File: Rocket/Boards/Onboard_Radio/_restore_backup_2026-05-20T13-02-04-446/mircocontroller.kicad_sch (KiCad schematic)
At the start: 32 parts, among them J3 USB_B_Micro, J4 SWD JST PH, U4 STM32H562RGT6, Y2 12MHz

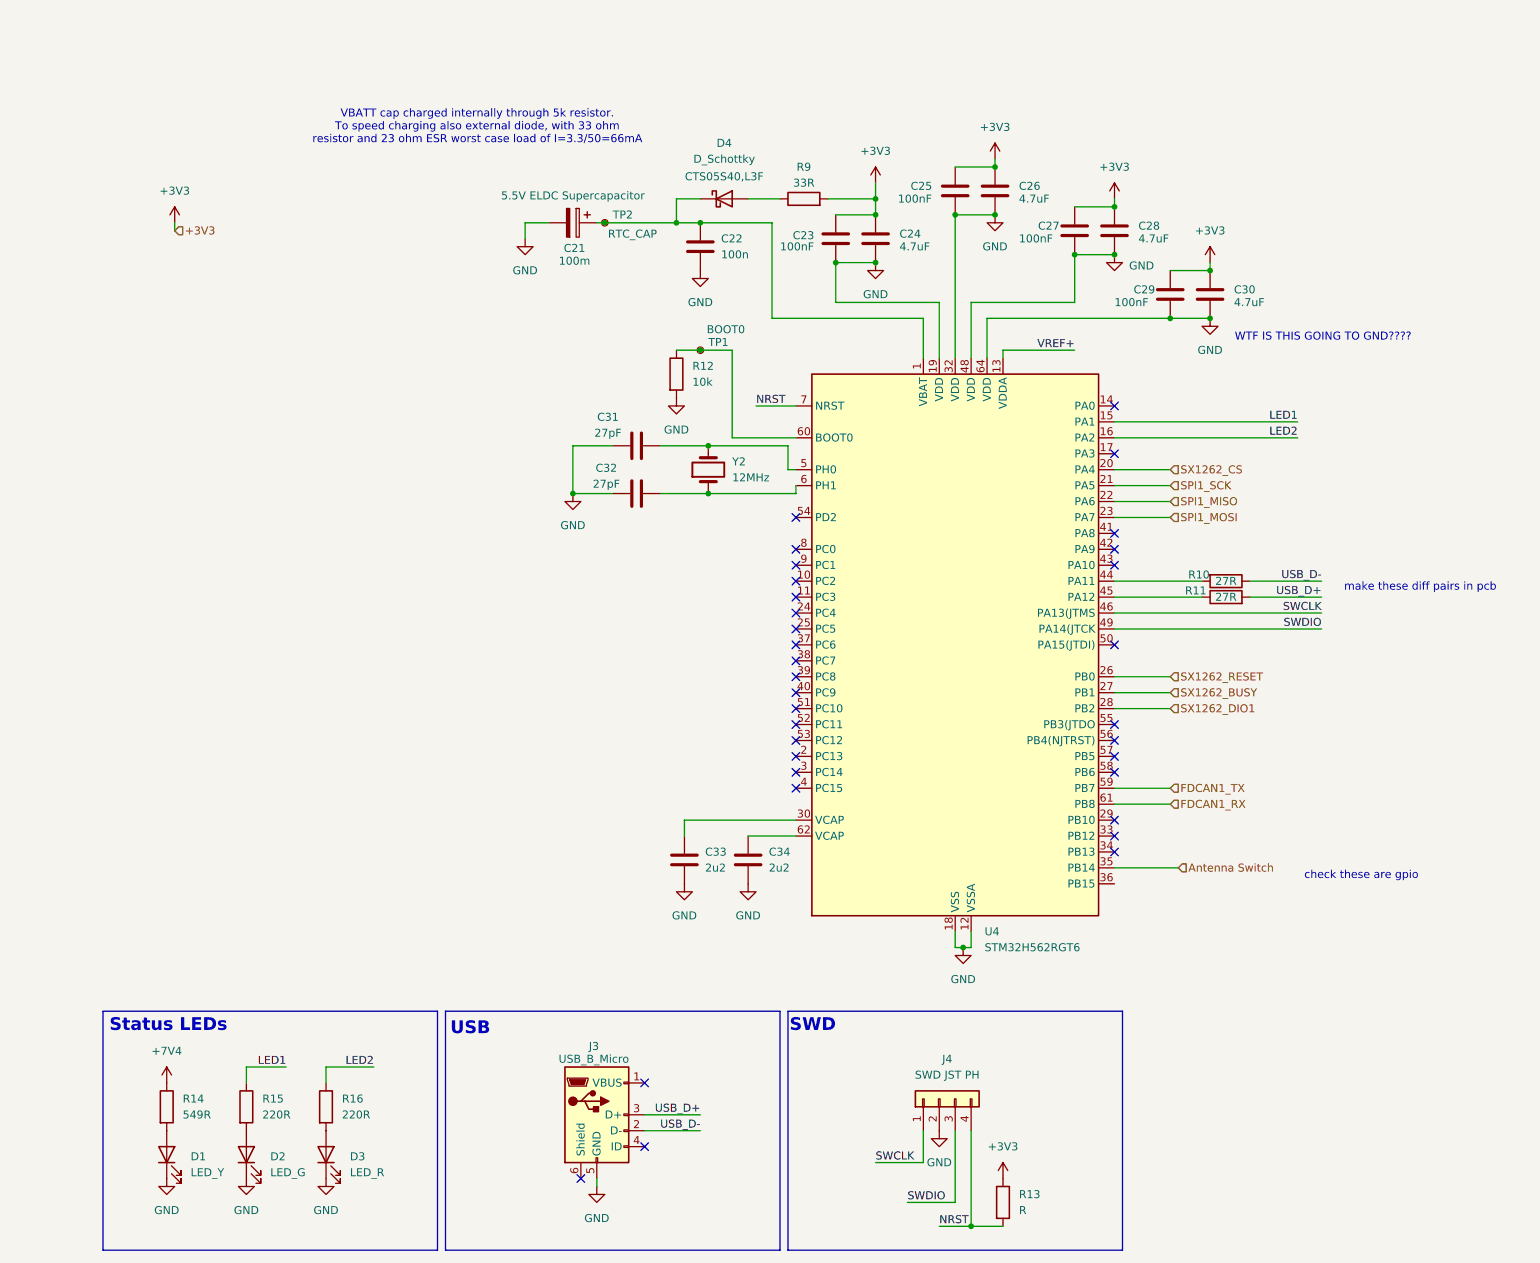
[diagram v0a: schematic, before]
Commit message: schematic bom needs updating and traces need finishing
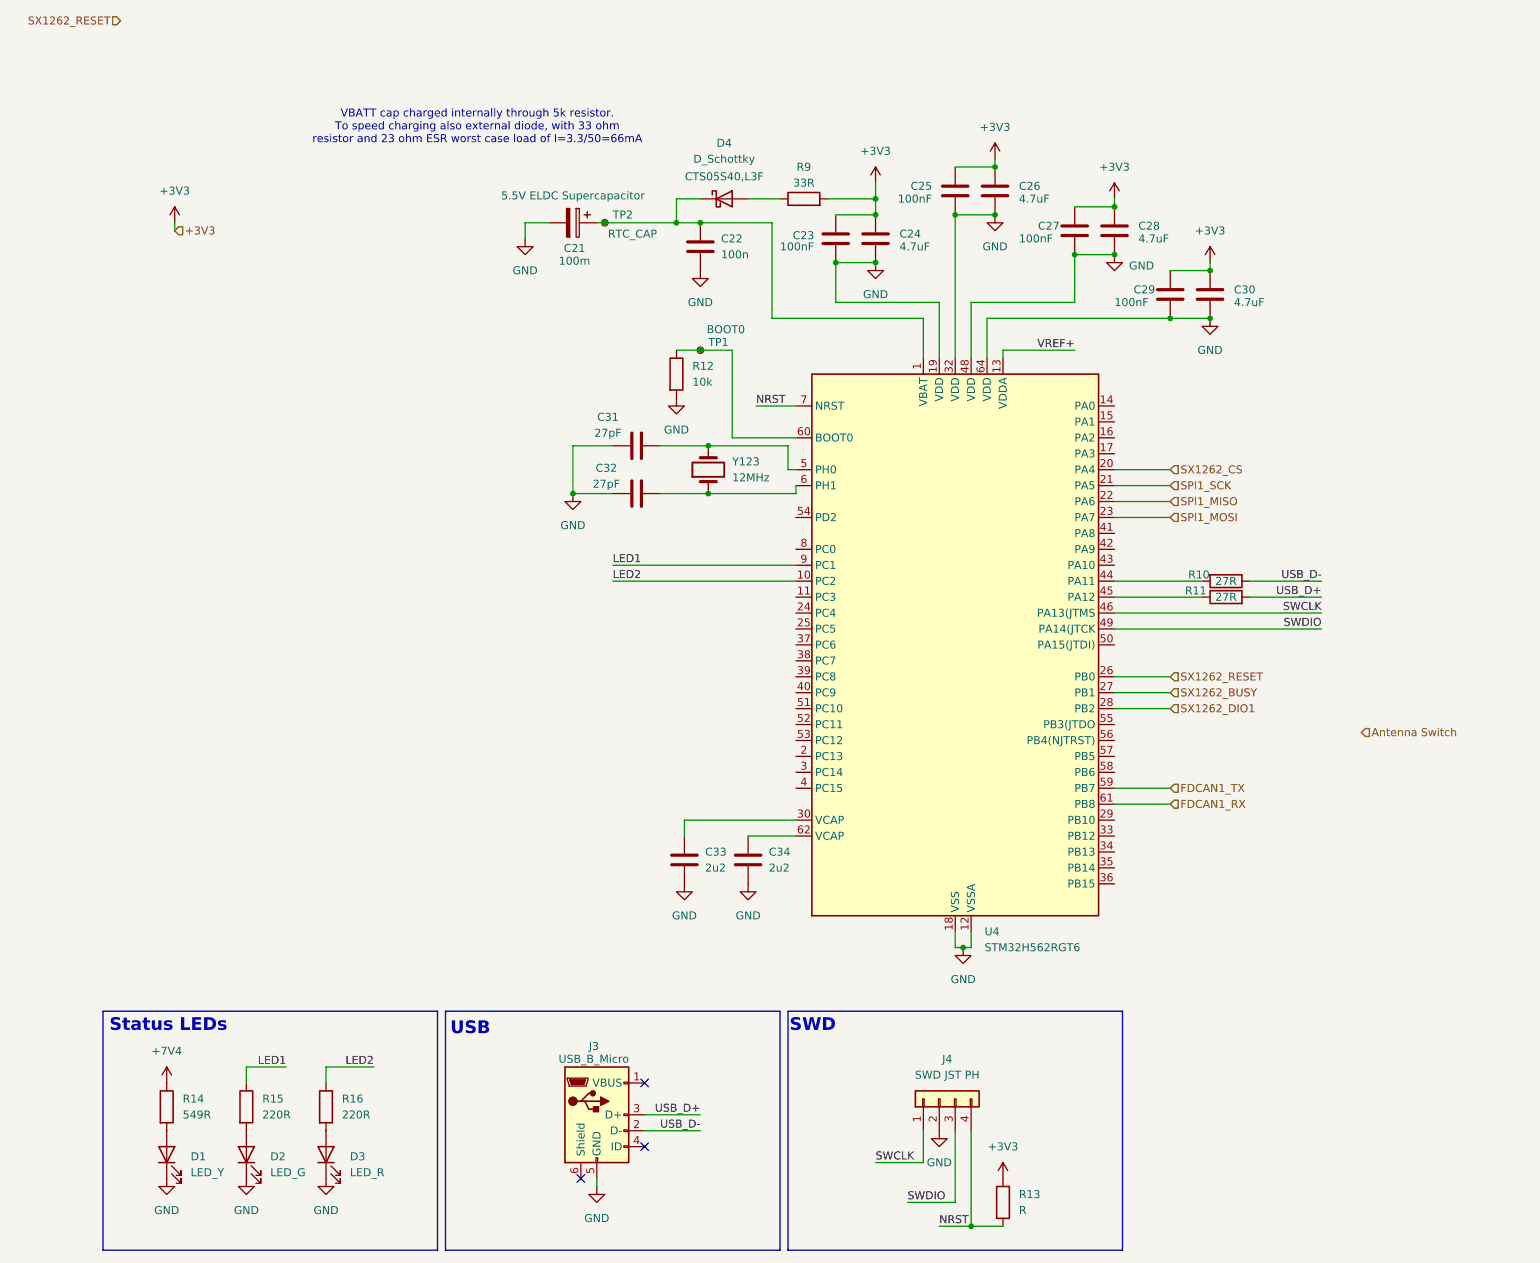
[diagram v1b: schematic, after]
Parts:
- renumbered Y2 to Y123
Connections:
- net Antenna Switch: no longer U4.35 (PB14)
- net LED1: now also U4.9 (PC1); no longer U4.15 (PA1)
- net LED2: now also U4.10 (PC2); no longer U4.16 (PA2)
- no-connect marks 33 -> 3
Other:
- note removed: "WTF IS THIS GOING TO GND????"
- note removed: "check these are gpio"
- note removed: "make these diff pairs in pcb"
